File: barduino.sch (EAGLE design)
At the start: 18 parts, among them Q2 16MHz, X1 MINI-USB-UX60A-MB-5ST

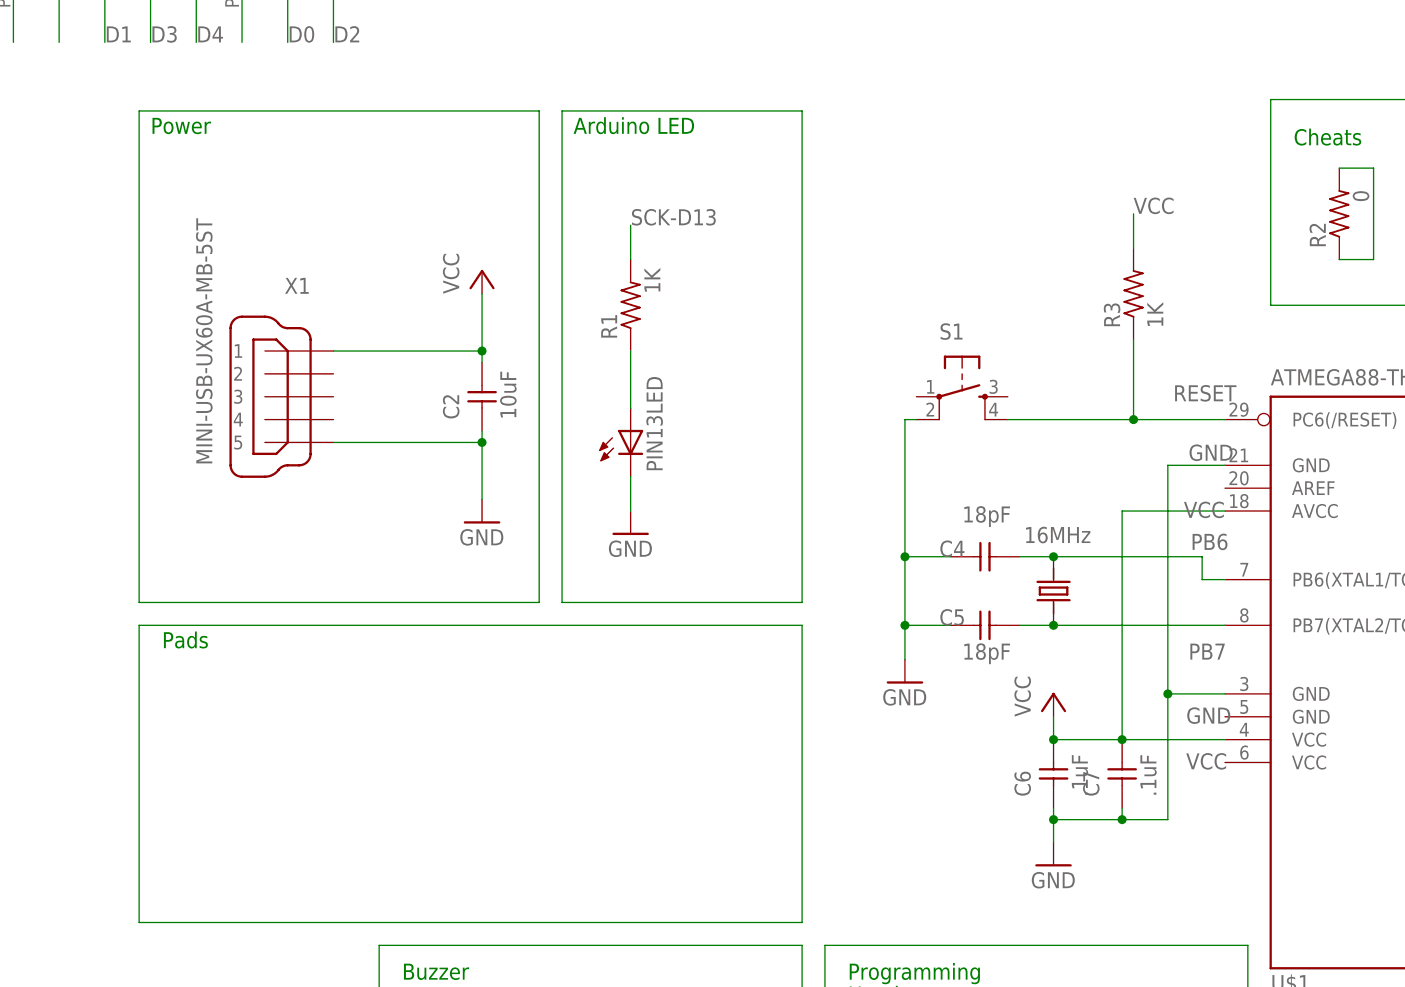
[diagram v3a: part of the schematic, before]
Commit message: remove reest button
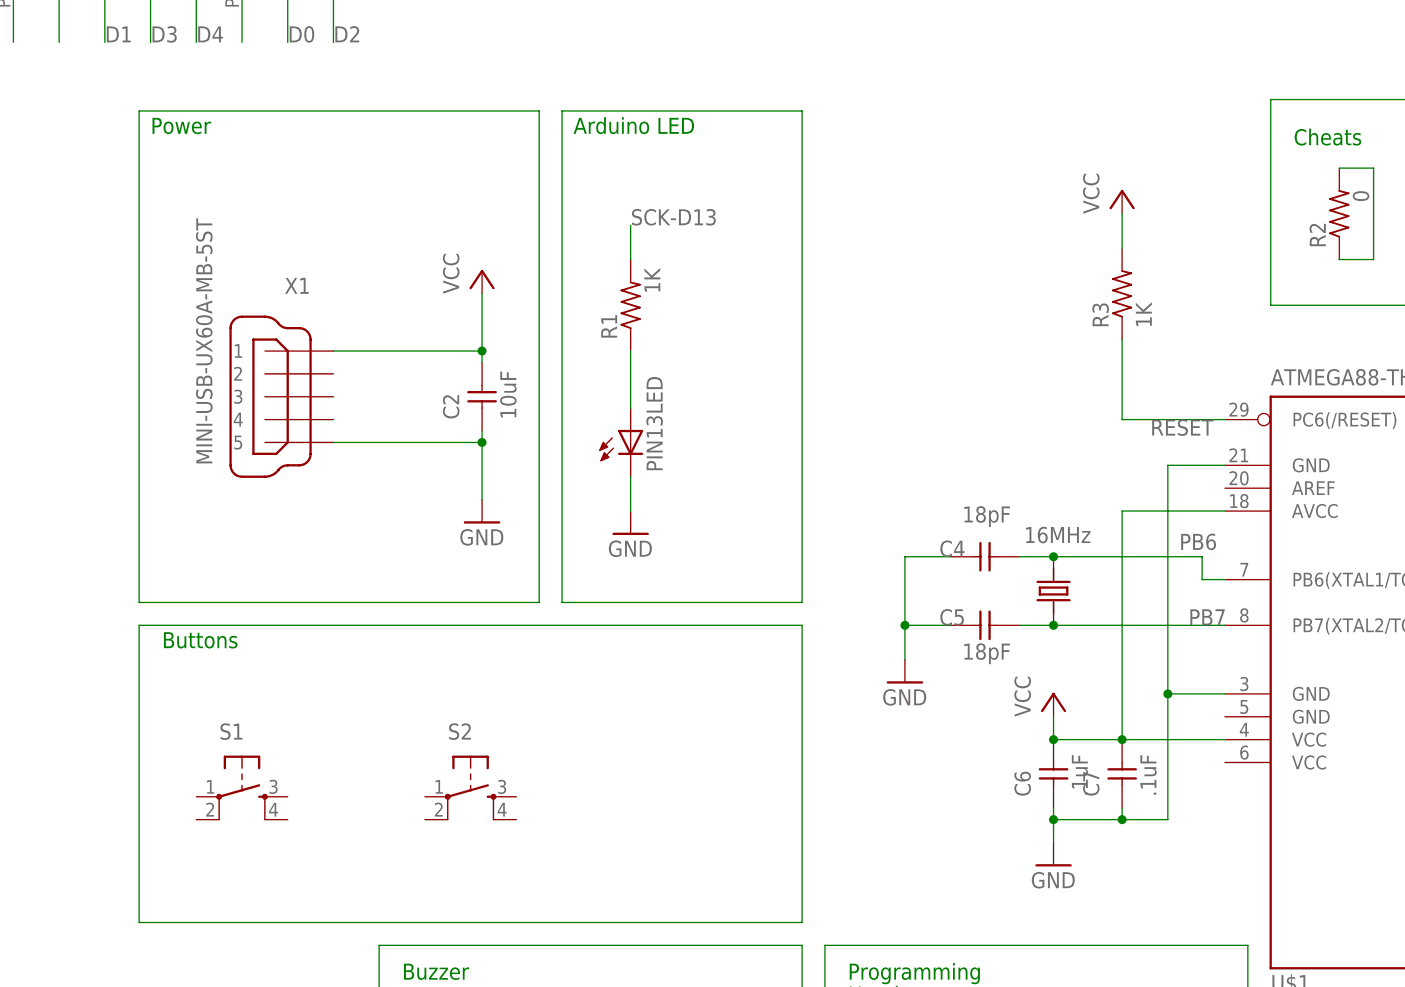
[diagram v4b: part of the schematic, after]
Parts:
- added S2: (no value), ng:6MM_SWITCH6MM_SWITCH
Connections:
- net GND: no longer S1.P1
- net RESET: no longer S1.S1
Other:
- note added: "Buttons"
- note removed: "Pads"
- moved on the sheet: R3, S1
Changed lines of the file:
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@@
 <part name="X1" library="con-hirose" library_urn="urn:adsk.eagle:library:152" deviceset="MINI-USB-" device="UX60A-MB-5ST"/>
 <part name="GND1" library="supply1" library_urn="urn:adsk.eagle:library:371" deviceset="GND" device=""/>
+<part name="P+1" library="supply1" library_urn="urn:adsk.eagle:library:371" deviceset="VCC" device=""/>
+<part name="S2" library="ng" deviceset="6MM_SWITCH" device="6MM_SWITCH"/>
 </parts>
 <sheets>
@@
 <plain>
 <text x="-50.8" y="128.27" size="1.778" layer="91">Power</text>
-<text x="-49.53" y="71.12" size="1.778" layer="91">Pads</text>
+<text x="-49.53" y="71.12" size="1.778" layer="91">Buttons</text>
 <text x="26.67" y="34.29" size="1.778" layer="91">Programming</text>
 <text x="26.67" y="31.75" size="1.778" layer="91">Header</text>
@@
 </instance>
 <instance part="C6" gate="1" x="49.53" y="58.42" rot="R90"/>
-<instance part="R3" gate="G$1" x="58.42" y="110.49" rot="R90"/>
+<instance part="R3" gate="G$1" x="57.15" y="110.49" rot="R90"/>
 <instance part="P+2" gate="VCC" x="-13.97" y="113.03"/>
-<instance part="S1" gate="2" x="39.37" y="99.06" rot="R270"/>
+<instance part="S1" gate="2" x="-40.64" y="54.61" rot="R270"/>
 <instance part="R1" gate="G$1" x="2.54" y="109.22" smashed="yes" rot="R90">
 <attribute name="NAME" x="1.0414" y="105.41" size="1.778" layer="95" rot="R90"/>
@@
 <instance part="X1" gate="G$1" x="-35.56" y="99.06" rot="MR0"/>
 <instance part="GND1" gate="1" x="-13.97" y="85.09"/>
+<instance part="P+1" gate="VCC" x="57.15" y="121.92"/>
+<instance part="S2" gate="2" x="-15.24" y="54.61" rot="R270"/>
 </instances>
 <busses>
@@
 <junction x="57.15" y="60.96"/>
 <junction x="49.53" y="60.96"/>
-<label x="64.262" y="57.658" size="1.778" layer="95"/>
-<label x="64.008" y="85.598" size="1.778" layer="95"/>
 <pinref part="P+3" gate="VCC" pin="VCC"/>
 <pinref part="C6" gate="1" pin="2"/>
@@
 </segment>
 <segment>
-<wire x1="58.42" y1="115.57" x2="58.42" y2="119.38" width="0.1524" layer="91"/>
-<label x="58.42" y="119.38" size="1.778" layer="95"/>
+<wire x1="57.15" y1="115.57" x2="57.15" y2="119.38" width="0.1524" layer="91"/>
 <pinref part="R3" gate="G$1" pin="2"/>
+<pinref part="P+1" gate="VCC" pin="VCC"/>
 </segment>
 <segment>
@@
 <junction x="62.23" y="66.04"/>
 <junction x="57.15" y="52.07"/>
-<label x="64.262" y="62.738" size="1.778" layer="95"/>
-<label x="64.516" y="91.948" size="1.778" layer="95"/>
 <pinref part="GND3" gate="1" pin="GND"/>
 <pinref part="C6" gate="1" pin="1"/>
@@
 <wire x1="33.02" y1="73.66" x2="33.02" y2="69.85" width="0.1524" layer="91"/>
 <wire x1="38.1" y1="73.66" x2="33.02" y2="73.66" width="0.1524" layer="91"/>
-<wire x1="34.29" y1="96.52" x2="33.02" y2="96.52" width="0.1524" layer="91"/>
-<wire x1="33.02" y1="96.52" x2="33.02" y2="81.28" width="0.1524" layer="91"/>
 <junction x="33.02" y="73.66"/>
-<junction x="33.02" y="81.28"/>
 <pinref part="GND4" gate="1" pin="GND"/>
 <pinref part="C4" gate="1" pin="1"/>
 <pinref part="C5" gate="1" pin="1"/>
-<pinref part="S1" gate="2" pin="P1"/>
 </segment>
 <segment>
@@
 <wire x1="68.58" y1="73.66" x2="49.53" y2="73.66" width="0.1524" layer="91"/>
 <junction x="49.53" y="73.66"/>
-<label x="64.516" y="69.85" size="1.778" layer="95"/>
+<label x="64.516" y="73.66" size="1.778" layer="95"/>
 <pinref part="Q2" gate="G$1" pin="1"/>
 <pinref part="C5" gate="1" pin="2"/>
@@
 <net name="RESET" class="0">
 <segment>
-<wire x1="58.42" y1="96.52" x2="58.42" y2="105.41" width="0.1524" layer="91"/>
-<wire x1="44.45" y1="96.52" x2="58.42" y2="96.52" width="0.1524" layer="91"/>
-<wire x1="68.58" y1="96.52" x2="58.42" y2="96.52" width="0.1524" layer="91"/>
-<junction x="58.42" y="96.52"/>
-<label x="69.85" y="100.33" size="1.778" layer="95" rot="R180"/>
+<wire x1="57.15" y1="96.52" x2="57.15" y2="105.41" width="0.1524" layer="91"/>
+<wire x1="68.58" y1="96.52" x2="57.15" y2="96.52" width="0.1524" layer="91"/>
+<label x="67.31" y="96.52" size="1.778" layer="95" rot="R180"/>
 <pinref part="R3" gate="G$1" pin="1"/>
-<pinref part="S1" gate="2" pin="S1"/>
 <pinref part="U$1" gate="G$1" pin="PC6(/RESET)"/>
 </segment>
@@
 <wire x1="68.58" y1="78.74" x2="66.04" y2="78.74" width="0.1524" layer="91"/>
 <junction x="49.53" y="81.28"/>
-<label x="64.77" y="82.042" size="1.778" layer="95"/>
+<label x="63.5" y="82.042" size="1.778" layer="95"/>
 <pinref part="Q2" gate="G$1" pin="2"/>
 <pinref part="C4" gate="1" pin="2"/>

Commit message: moving things
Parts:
- removed PIN13LED: (no value), ng:LED1206
- removed R1: 1K, ng:RESISTOR1206
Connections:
- removed net N$26: R2.1, R2.2
- removed net N$4: PIN13LED.A, R1.1
- net GND: no longer PIN13LED.C
- net SCK-D13: now also R2.1, R2.2; no longer R1.2
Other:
- note removed: "Arduino LED"
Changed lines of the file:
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@@
 <part name="P+2" library="supply1" deviceset="VCC" device=""/>
 <part name="S1" library="ng" deviceset="6MM_SWITCH" device="6MM_SWITCH"/>
-<part name="R1" library="ng" deviceset="RESISTOR" device="1206" value="1K"/>
-<part name="PIN13LED" library="ng" deviceset="LED" device="1206"/>
 <part name="C2" library="ng" deviceset="UNPOLARIZED_CAPACITOR" device="1206" value="10uF"/>
-<part name="GND5" library="supply1" deviceset="GND" device=""/>
 <part name="C7" library="ng" deviceset="UNPOLARIZED_CAPACITOR" device="1206" value=".1uF"/>
 <part name="U$1" library="fab" deviceset="ATMEGA88-THIN" device=""/>
@@
 <part name="P+1" library="supply1" library_urn="urn:adsk.eagle:library:371" deviceset="VCC" device=""/>
 <part name="S2" library="ng" deviceset="6MM_SWITCH" device="6MM_SWITCH"/>
+<part name="P+4" library="supply1" library_urn="urn:adsk.eagle:library:371" deviceset="VCC" device=""/>
+<part name="GND5" library="supply1" library_urn="urn:adsk.eagle:library:371" deviceset="GND" device=""/>
 </parts>
 <sheets>
@@
 <text x="76.2" y="127" size="1.778" layer="91">Cheats</text>
 <text x="-22.86" y="34.29" size="1.778" layer="91">Buzzer</text>
-<text x="-3.81" y="128.27" size="1.778" layer="91">Arduino LED</text>
 </plain>
 <instances>
@@
 <instance part="P+2" gate="VCC" x="-13.97" y="113.03"/>
 <instance part="S1" gate="2" x="-40.64" y="54.61" rot="R270"/>
-<instance part="R1" gate="G$1" x="2.54" y="109.22" smashed="yes" rot="R90">
-<attribute name="NAME" x="1.0414" y="105.41" size="1.778" layer="95" rot="R90"/>
-<attribute name="VALUE" x="5.842" y="110.49" size="1.778" layer="96" rot="R90"/>
-</instance>
-<instance part="PIN13LED" gate="G$1" x="2.54" y="92.71"/>
 <instance part="C2" gate="1" x="-13.97" y="100.33" rot="R90"/>
-<instance part="GND5" gate="1" x="2.54" y="83.82"/>
 <instance part="C7" gate="1" x="57.15" y="58.42" rot="R90"/>
 <instance part="U$1" gate="G$1" x="91.44" y="71.12"/>
@@
 <instance part="P+1" gate="VCC" x="57.15" y="121.92"/>
 <instance part="S2" gate="2" x="-15.24" y="54.61" rot="R270"/>
+<instance part="P+4" gate="VCC" x="58.42" y="34.29"/>
+<instance part="GND5" gate="1" x="58.42" y="12.7"/>
 </instances>
 <busses>
@@
 </segment>
 <segment>
-<wire x1="48.26" y1="22.86" x2="58.42" y2="22.86" width="0.1524" layer="91"/>
-<label x="58.42" y="22.86" size="1.778" layer="95"/>
-<pinref part="ICSP" gate="A" pin="2"/>
-</segment>
-<segment>
 <wire x1="-13.97" y1="104.14" x2="-13.97" y2="102.87" width="0.1524" layer="91"/>
 <wire x1="-13.97" y1="110.49" x2="-13.97" y2="104.14" width="0.1524" layer="91"/>
@@
 <pinref part="R7" gate="G$1" pin="2"/>
 <wire x1="107.95" y1="124.46" x2="104.14" y2="124.46" width="0.1524" layer="91"/>
+</segment>
+<segment>
+<pinref part="ICSP" gate="A" pin="2"/>
+<wire x1="48.26" y1="22.86" x2="58.42" y2="22.86" width="0.1524" layer="91"/>
+<wire x1="58.42" y1="22.86" x2="58.42" y2="31.75" width="0.1524" layer="91"/>
+<pinref part="P+4" gate="VCC" pin="VCC"/>
 </segment>
 </net>
@@
 </segment>
 <segment>
-<wire x1="2.54" y1="90.17" x2="2.54" y2="86.36" width="0.1524" layer="91"/>
-<pinref part="PIN13LED" gate="G$1" pin="C"/>
-<pinref part="GND5" gate="1" pin="GND"/>
-</segment>
-<segment>
-<wire x1="48.26" y1="17.78" x2="58.42" y2="17.78" width="0.1524" layer="91"/>
-<label x="58.42" y="17.78" size="1.778" layer="95"/>
-<pinref part="ICSP" gate="A" pin="6"/>
-</segment>
-<segment>
 <pinref part="SG1" gate="G$1" pin="2"/>
 <pinref part="GND2" gate="1" pin="GND"/>
@@
 <wire x1="-13.97" y1="87.63" x2="-13.97" y2="93.98" width="0.1524" layer="91"/>
 <junction x="-13.97" y="93.98"/>
+</segment>
+<segment>
+<pinref part="ICSP" gate="A" pin="6"/>
+<wire x1="48.26" y1="17.78" x2="58.42" y2="17.78" width="0.1524" layer="91"/>
+<wire x1="58.42" y1="17.78" x2="58.42" y2="15.24" width="0.1524" layer="91"/>
+<pinref part="GND5" gate="1" pin="GND"/>
 </segment>
 </net>
@@
 </segment>
 </net>
-<net name="N$4" class="0">
-<segment>
-<wire x1="2.54" y1="97.79" x2="2.54" y2="104.14" width="0.1524" layer="91"/>
-<pinref part="R1" gate="G$1" pin="1"/>
-<pinref part="PIN13LED" gate="G$1" pin="A"/>
-</segment>
-</net>
 <net name="A1" class="0">
 <segment>
@@
 <net name="SCK-D13" class="0">
 <segment>
-<wire x1="2.54" y1="114.3" x2="2.54" y2="118.11" width="0.1524" layer="91"/>
-<label x="2.54" y="118.11" size="1.778" layer="95"/>
-<pinref part="R1" gate="G$1" pin="2"/>
-</segment>
-<segment>
 <wire x1="116.84" y1="38.1" x2="121.92" y2="38.1" width="0.1524" layer="91"/>
 <label x="121.92" y="38.1" size="1.778" layer="95"/>
@@
 <label x="25.4" y="20.32" size="1.778" layer="95"/>
 <pinref part="ICSP" gate="A" pin="3"/>
+</segment>
+<segment>
+<pinref part="R2" gate="G$1" pin="1"/>
+<wire x1="81.28" y1="114.3" x2="85.09" y2="114.3" width="0.1524" layer="91"/>
+<wire x1="85.09" y1="114.3" x2="85.09" y2="124.46" width="0.1524" layer="91"/>
+<pinref part="R2" gate="G$1" pin="2"/>
+<wire x1="85.09" y1="124.46" x2="81.28" y2="124.46" width="0.1524" layer="91"/>
 </segment>
 </net>
@@
 </segment>
 </net>
-<net name="N$26" class="0">
-<segment>
-<pinref part="R2" gate="G$1" pin="1"/>
-<wire x1="81.28" y1="114.3" x2="85.09" y2="114.3" width="0.1524" layer="91"/>
-<wire x1="85.09" y1="114.3" x2="85.09" y2="124.46" width="0.1524" layer="91"/>
-<pinref part="R2" gate="G$1" pin="2"/>
-<wire x1="85.09" y1="124.46" x2="81.28" y2="124.46" width="0.1524" layer="91"/>
-</segment>
-</net>
-<net name="N$1" class="0">
-<segment>
-<wire x1="-5.08" y1="130.81" x2="-5.08" y2="76.2" width="0.1524" layer="91"/>
-<wire x1="-5.08" y1="76.2" x2="21.59" y2="76.2" width="0.1524" layer="91"/>
-<wire x1="21.59" y1="76.2" x2="21.59" y2="130.81" width="0.1524" layer="91"/>
-<wire x1="21.59" y1="130.81" x2="-5.08" y2="130.81" width="0.1524" layer="91"/>
-</segment>
-</net>
